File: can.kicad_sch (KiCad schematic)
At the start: 11 parts, among them U2 SN65HVD230

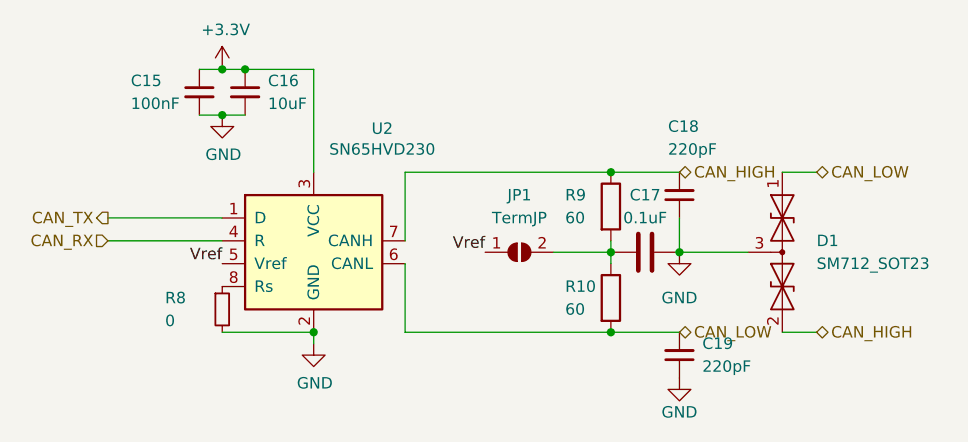
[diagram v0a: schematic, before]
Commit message: changed capacitor value and resistor footprints
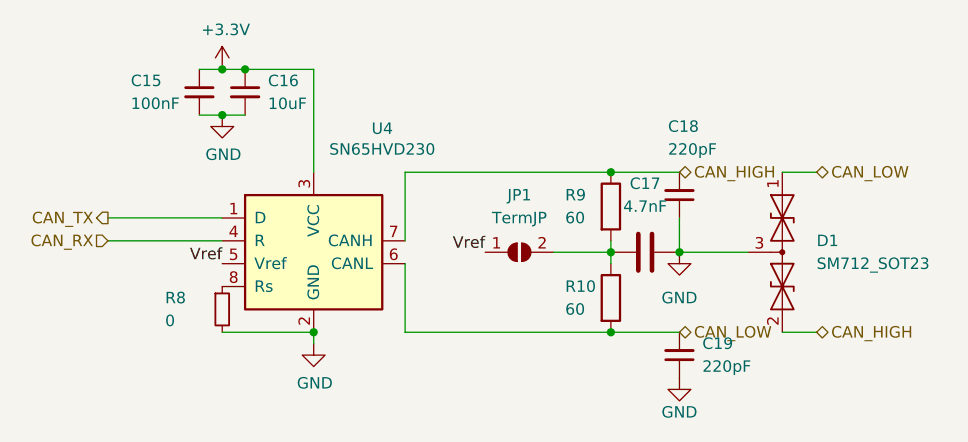
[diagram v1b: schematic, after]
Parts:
- C17: value 0.1uF -> 4.7nF
- JP1: footprint (none) -> Jumper:SolderJumper-2_P1.3mm_Open_RoundedPad1.0x1.5mm
- R10, R9: footprint Resistor_SMD:R_0402_1005Metric -> Resistor_SMD:R_0603_1608Metric
- renumbered U2 to U4
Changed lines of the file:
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@@
   (symbol (lib_id "power:GND") (at 134.62 99.06 0) (unit 1)
     (in_bom yes) (on_board yes) (fields_autoplaced)
-    (property "Reference" "#PWR026" (id 0) (at 134.62 105.41 0)
+    (property "Reference" "#PWR0130" (id 0) (at 134.62 105.41 0)
       (effects (font (size 1.27 1.27)) hide)
     )
@@
   (symbol (lib_id "power:+3.3V") (at 124.46 68.58 0) (unit 1)
     (in_bom yes) (on_board yes) (fields_autoplaced)
-    (property "Reference" "#PWR024" (id 0) (at 124.46 72.39 0)
+    (property "Reference" "#PWR0131" (id 0) (at 124.46 72.39 0)
       (effects (font (size 1.27 1.27)) hide)
     )
@@
   (symbol (lib_id "Interface_CAN_LIN:SN65HVD230") (at 134.62 87.63 0) (unit 1)
     (in_bom yes) (on_board yes) (fields_autoplaced)
-    (property "Reference" "U2" (id 0) (at 142.24 75.1586 0))
+    (property "Reference" "U4" (id 0) (at 142.24 75.1586 0))
     (property "Value" "SN65HVD230" (id 1) (at 142.24 77.47 0))
     (property "Footprint" "Package_SO:SOIC-8_3.9x4.9mm_P1.27mm" (id 2) (at 134.62 100.33 0)
@@
       (effects (font (size 1.27 1.27)) (justify left))
     )
-    (property "Footprint" "Resistor_SMD:R_0402_1005Metric" (id 2) (at 165.862 93.98 90)
+    (property "Footprint" "Resistor_SMD:R_0603_1608Metric" (id 2) (at 165.862 93.98 90)
       (effects (font (size 1.27 1.27)) hide)
     )
@@
       (effects (font (size 1.27 1.27)) (justify left))
     )
-    (property "Footprint" "Resistor_SMD:R_0402_1005Metric" (id 2) (at 165.862 83.82 90)
+    (property "Footprint" "Resistor_SMD:R_0603_1608Metric" (id 2) (at 165.862 83.82 90)
       (effects (font (size 1.27 1.27)) hide)
     )
@@
   (symbol (lib_id "Device:C") (at 171.45 88.9 90) (unit 1)
     (in_bom yes) (on_board yes) (fields_autoplaced)
-    (property "Reference" "C17" (id 0) (at 171.45 82.55 90))
-    (property "Value" "0.1uF" (id 1) (at 171.45 85.09 90))
+    (property "Reference" "C17" (id 0) (at 171.45 81.28 90))
+    (property "Value" "4.7nF" (id 1) (at 171.45 83.82 90))
     (property "Footprint" "Capacitor_SMD:C_0402_1005Metric" (id 2) (at 175.26 87.9348 0)
       (effects (font (size 1.27 1.27)) hide)
@@
     (property "Reference" "JP1" (id 0) (at 157.48 82.55 0))
     (property "Value" "TermJP" (id 1) (at 157.48 85.09 0))
-    (property "Footprint" "" (id 2) (at 157.48 88.9 0)
+    (property "Footprint" "Jumper:SolderJumper-2_P1.3mm_Open_RoundedPad1.0x1.5mm" (id 2) (at 157.48 88.9 0)
       (effects (font (size 1.27 1.27)) hide)
     )
@@
   )
   (symbol_instances
+    (path "/d85aebac-c325-42de-8c8e-5349542a2954"
+      (reference "#PWR025") (unit 1) (value "GND") (footprint "")
+    )
+    (path "/49208f5a-f73e-42f1-9d7d-382d975bd991"
+      (reference "#PWR027") (unit 1) (value "GND") (footprint "")
+    )
+    (path "/54c27e2d-52b9-4197-956b-7db5f761b4df"
+      (reference "#PWR028") (unit 1) (value "GND") (footprint "")
+    )
     (path "/00000000-0000-0000-0000-000061946eb3"
       (reference "#PWR0130") (unit 1) (value "GND") (footprint "")
@@
       (reference "#PWR0131") (unit 1) (value "+3.3V") (footprint "")
     )
+    (path "/759646bf-5c31-420e-aff7-2c1a28ce32e1"
+      (reference "C15") (unit 1) (value "100nF") (footprint "Capacitor_SMD:C_0402_1005Metric")
+    )
+    (path "/06b0d844-1c7a-43fd-b8a5-ad8e34e13aac"
+      (reference "C16") (unit 1) (value "10uF") (footprint "Capacitor_SMD:C_0402_1005Metric")
+    )
+    (path "/c905e3f6-13b1-4d5f-8bb5-930cfa107996"
+      (reference "C17") (unit 1) (value "4.7nF") (footprint "Capacitor_SMD:C_0402_1005Metric")
+    )
+    (path "/23622c20-4a70-4ee7-b39c-f5519633413f"
+      (reference "C18") (unit 1) (value "220pF") (footprint "Capacitor_SMD:C_0402_1005Metric")
+    )
+    (path "/f5a97da1-282d-43a4-ae5f-607cebde55a6"
+      (reference "C19") (unit 1) (value "220pF") (footprint "Capacitor_SMD:C_0402_1005Metric")
+    )
+    (path "/4717c16e-4caf-41db-976f-f247d2a86ecc"
+      (reference "D1") (unit 1) (value "SM712_SOT23") (footprint "Package_TO_SOT_SMD:SOT-23")
+    )
+    (path "/deb2b25e-9fb0-448e-88c5-95a67db1d371"
+      (reference "JP1") (unit 1) (value "TermJP") (footprint "Jumper:SolderJumper-2_P1.3mm_Open_RoundedPad1.0x1.5mm")
+    )
+    (path "/c0a35b75-0e83-4311-add3-5a3930110d30"
+      (reference "R8") (unit 1) (value "0") (footprint "Resistor_SMD:R_0603_1608Metric")
+    )
+    (path "/c4e42d16-8dbe-42af-a61a-faa72b95fe53"
+      (reference "R9") (unit 1) (value "60") (footprint "Resistor_SMD:R_0603_1608Metric")
+    )
+    (path "/c363df37-be76-44cd-846e-5e1010ee0d3e"
+      (reference "R10") (unit 1) (value "60") (footprint "Resistor_SMD:R_0603_1608Metric")
+    )
     (path "/00000000-0000-0000-0000-000061946ec3"

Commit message: changed usb port footprint to the combined SMD/THT one
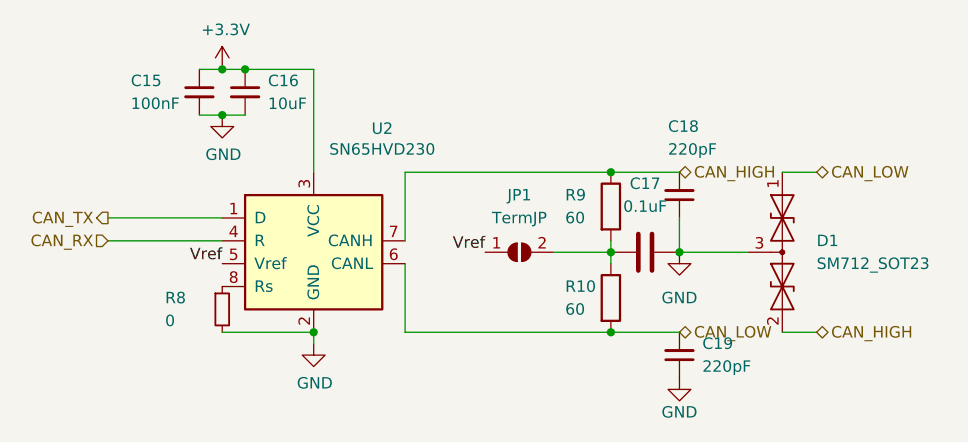
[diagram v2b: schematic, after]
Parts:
- C17: value 4.7nF -> 0.1uF
- R10, R9: footprint Resistor_SMD:R_0603_1608Metric -> Resistor_SMD:R_0402_1005Metric
- renumbered U4 to U2
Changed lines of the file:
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@@
   (symbol (lib_id "power:GND") (at 134.62 99.06 0) (unit 1)
     (in_bom yes) (on_board yes) (fields_autoplaced)
-    (property "Reference" "#PWR0130" (id 0) (at 134.62 105.41 0)
+    (property "Reference" "#PWR026" (id 0) (at 134.62 105.41 0)
       (effects (font (size 1.27 1.27)) hide)
     )
@@
   (symbol (lib_id "power:+3.3V") (at 124.46 68.58 0) (unit 1)
     (in_bom yes) (on_board yes) (fields_autoplaced)
-    (property "Reference" "#PWR0131" (id 0) (at 124.46 72.39 0)
+    (property "Reference" "#PWR024" (id 0) (at 124.46 72.39 0)
       (effects (font (size 1.27 1.27)) hide)
     )
@@
   (symbol (lib_id "Interface_CAN_LIN:SN65HVD230") (at 134.62 87.63 0) (unit 1)
     (in_bom yes) (on_board yes) (fields_autoplaced)
-    (property "Reference" "U4" (id 0) (at 142.24 75.1586 0))
+    (property "Reference" "U2" (id 0) (at 142.24 75.1586 0))
     (property "Value" "SN65HVD230" (id 1) (at 142.24 77.47 0))
     (property "Footprint" "Package_SO:SOIC-8_3.9x4.9mm_P1.27mm" (id 2) (at 134.62 100.33 0)
@@
       (effects (font (size 1.27 1.27)) (justify left))
     )
-    (property "Footprint" "Resistor_SMD:R_0603_1608Metric" (id 2) (at 165.862 93.98 90)
+    (property "Footprint" "Resistor_SMD:R_0402_1005Metric" (id 2) (at 165.862 93.98 90)
       (effects (font (size 1.27 1.27)) hide)
     )
@@
       (effects (font (size 1.27 1.27)) (justify left))
     )
-    (property "Footprint" "Resistor_SMD:R_0603_1608Metric" (id 2) (at 165.862 83.82 90)
+    (property "Footprint" "Resistor_SMD:R_0402_1005Metric" (id 2) (at 165.862 83.82 90)
       (effects (font (size 1.27 1.27)) hide)
     )
@@
     (in_bom yes) (on_board yes) (fields_autoplaced)
     (property "Reference" "C17" (id 0) (at 171.45 81.28 90))
-    (property "Value" "4.7nF" (id 1) (at 171.45 83.82 90))
+    (property "Value" "0.1uF" (id 1) (at 171.45 83.82 90))
     (property "Footprint" "Capacitor_SMD:C_0402_1005Metric" (id 2) (at 175.26 87.9348 0)
       (effects (font (size 1.27 1.27)) hide)

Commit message: updated some schematic values
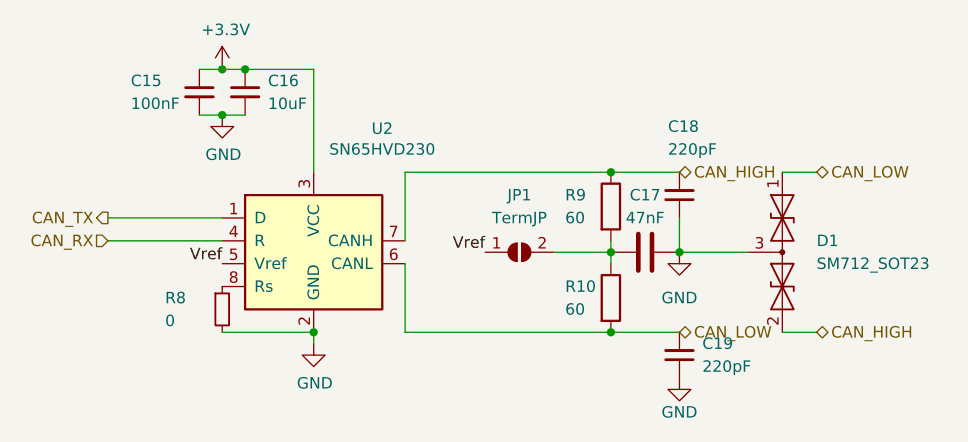
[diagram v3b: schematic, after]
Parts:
- C17: value 0.1uF -> 47nF
- R10, R9: footprint Resistor_SMD:R_0402_1005Metric -> Resistor_SMD:R_0603_1608Metric

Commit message: implemented fixes that were changed for ordering of nimbus flight electronics, tidied up layout and set up manufacturing constraints
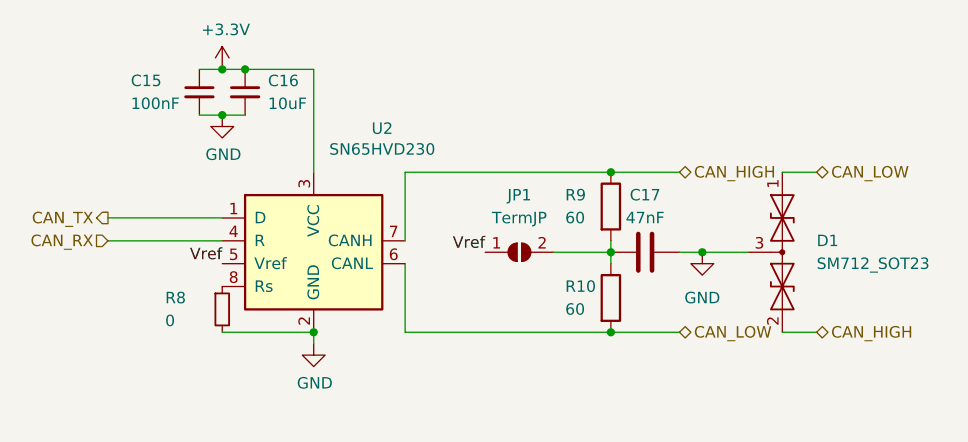
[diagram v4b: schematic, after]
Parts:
- removed C18, C19: 220pF, Capacitor_SMD:C_0402_1005Metric, symbol Device:C_Small
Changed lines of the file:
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@@
   (junction (at 167.64 80.01) (diameter 0) (color 0 0 0 0)
   )
-  (junction (at 175.26 88.9) (diameter 0) (color 0 0 0 0)
+  (junction (at 177.8 88.9) (diameter 0) (color 0 0 0 0)
   )
   (junction (at 167.64 97.79) (diameter 0) (color 0 0 0 0)
@@
     (stroke (width 0) (type default))
   )
+  (wire (pts (xy 177.8 88.9) (xy 182.88 88.9))
+    (stroke (width 0) (type default))
+  )
   (wire (pts (xy 121.92 73.66) (xy 124.46 73.66))
     (stroke (width 0) (type default))
@@
     (stroke (width 0) (type default))
   )
-  (wire (pts (xy 175.26 85.09) (xy 175.26 88.9))
-    (stroke (width 0) (type default))
-  )
   (wire (pts (xy 124.46 68.58) (xy 127 68.58))
     (stroke (width 0) (type default))
   )
-  (wire (pts (xy 175.26 88.9) (xy 182.88 88.9))
-    (stroke (width 0) (type default))
-  )
   (wire (pts (xy 111.76 87.63) (xy 124.46 87.63))
     (stroke (width 0) (type default))
@@
   )
   (wire (pts (xy 144.78 87.63) (xy 144.78 80.01))
+    (stroke (width 0) (type default))
+  )
+  (wire (pts (xy 177.8 88.9) (xy 175.26 88.9))
     (stroke (width 0) (type default))
   )
@@
     )
   )
-  (symbol (lib_id "Device:C_Small") (at 175.26 82.55 180) (unit 1)
-    (in_bom yes) (on_board yes) (dnp no)
-    (property "Reference" "C18" (at 173.99 74.93 0)
-      (effects (font (size 1.27 1.27)) (justify right))
-    )
-    (property "Value" "220pF" (at 173.99 77.47 0)
-      (effects (font (size 1.27 1.27)) (justify right))
-    )
-    (property "Footprint" "Capacitor_SMD:C_0402_1005Metric" (at 175.26 82.55 0)
-      (effects (font (size 1.27 1.27)) hide)
-    )
-    (property "Datasheet" "~" (at 175.26 82.55 0)
-      (effects (font (size 1.27 1.27)) hide)
-    )
-    (pin "1")
-    (pin "2")
-    (instances
-      (project "RicardoTemplate"
-        (path "/7db990e4-92e1-4f99-b4d2-435bbec1ba83/00000000-0000-0000-0000-000061942b9a"
-          (reference "C18") (unit 1)
-        )
-      )
-    )
-  )
   (symbol (lib_id "Diode:SM712_SOT23") (at 186.69 88.9 270) (unit 1)
     (in_bom yes) (on_board yes) (dnp no) (fields_autoplaced)
@@
     )
   )
-  (symbol (lib_id "power:GND") (at 175.26 88.9 0) (unit 1)
-    (in_bom yes) (on_board yes) (dnp no) (fields_autoplaced)
-    (property "Reference" "#PWR027" (at 175.26 95.25 0)
-      (effects (font (size 1.27 1.27)) hide)
-    )
-    (property "Value" "GND" (at 175.26 93.98 0)
-      (effects (font (size 1.27 1.27)))
-    )
-    (property "Footprint" "" (at 175.26 88.9 0)
-      (effects (font (size 1.27 1.27)) hide)
-    )
-    (property "Datasheet" "" (at 175.26 88.9 0)
+  (symbol (lib_id "power:GND") (at 177.8 88.9 0) (unit 1)
+    (in_bom yes) (on_board yes) (dnp no) (fields_autoplaced)
+    (property "Reference" "#PWR027" (at 177.8 95.25 0)
+      (effects (font (size 1.27 1.27)) hide)
+    )
+    (property "Value" "GND" (at 177.8 93.98 0)
+      (effects (font (size 1.27 1.27)))
+    )
+    (property "Footprint" "" (at 177.8 88.9 0)
+      (effects (font (size 1.27 1.27)) hide)
+    )
+    (property "Datasheet" "" (at 177.8 88.9 0)
       (effects (font (size 1.27 1.27)) hide)
     )
@@
         (path "/7db990e4-92e1-4f99-b4d2-435bbec1ba83/00000000-0000-0000-0000-000061942b9a"
           (reference "#PWR027") (unit 1)
-        )
-      )
-    )
-  )
-  (symbol (lib_id "power:GND") (at 175.26 102.87 0) (unit 1)
-    (in_bom yes) (on_board yes) (dnp no) (fields_autoplaced)
-    (property "Reference" "#PWR028" (at 175.26 109.22 0)
-      (effects (font (size 1.27 1.27)) hide)
-    )
-    (property "Value" "GND" (at 175.26 106.68 0)
-      (effects (font (size 1.27 1.27)))
-    )
-    (property "Footprint" "" (at 175.26 102.87 0)
-      (effects (font (size 1.27 1.27)) hide)
-    )
-    (property "Datasheet" "" (at 175.26 102.87 0)
-      (effects (font (size 1.27 1.27)) hide)
-    )
-    (pin "1")
-    (instances
-      (project "RicardoTemplate"
-        (path "/7db990e4-92e1-4f99-b4d2-435bbec1ba83/00000000-0000-0000-0000-000061942b9a"
-          (reference "#PWR028") (unit 1)
         )
       )
@@
         )
       )
-    )
-  )
-  (symbol (lib_id "Device:C_Small") (at 175.26 100.33 180) (unit 1)
-    (in_bom yes) (on_board yes) (dnp no) (fields_autoplaced)
-    (property "Reference" "C19" (at 177.8 99.0535 0)
-      (effects (font (size 1.27 1.27)) (justify right))
-    )
-    (property "Value" "220pF" (at 177.8 101.5935 0)
-      (effects (font (size 1.27 1.27)) (justify right))
-    )
-    (property "Footprint" "Capacitor_SMD:C_0402_1005Metric" (at 175.26 100.33 0)
-      (effects (font (size 1.27 1.27)) hide)
-    )
-    (property "Datasheet" "~" (at 175.26 100.33 0)
-      (effects (font (size 1.27 1.27)) hide)
-    )
-    (pin "1")
-    (pin "2")
-    (instances
-      (project "RicardoTemplate"
-        (path "/7db990e4-92e1-4f99-b4d2-435bbec1ba83/00000000-0000-0000-0000-000061942b9a"
-          (reference "C19") (unit 1)
-        )
-      )

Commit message: Added CAN LEDs and some general fixes noticed over the year
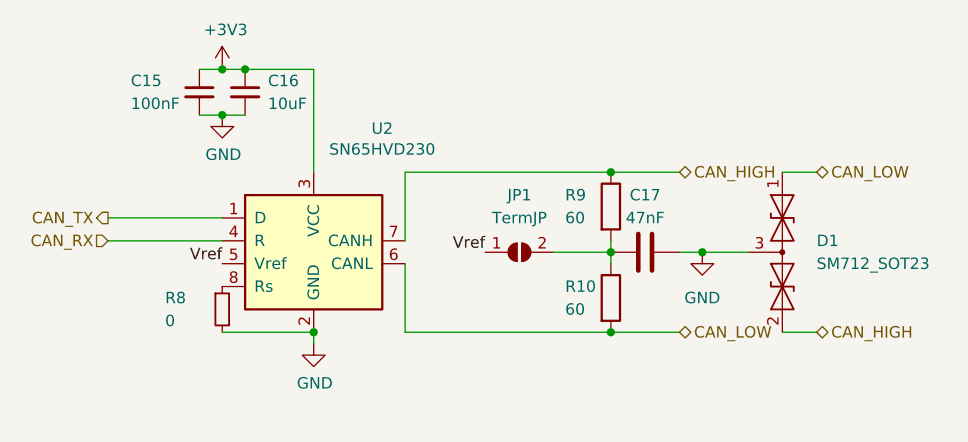
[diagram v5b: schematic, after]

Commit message: Fixed LED footprints assigned as resistors, added gitignore for locks and backups
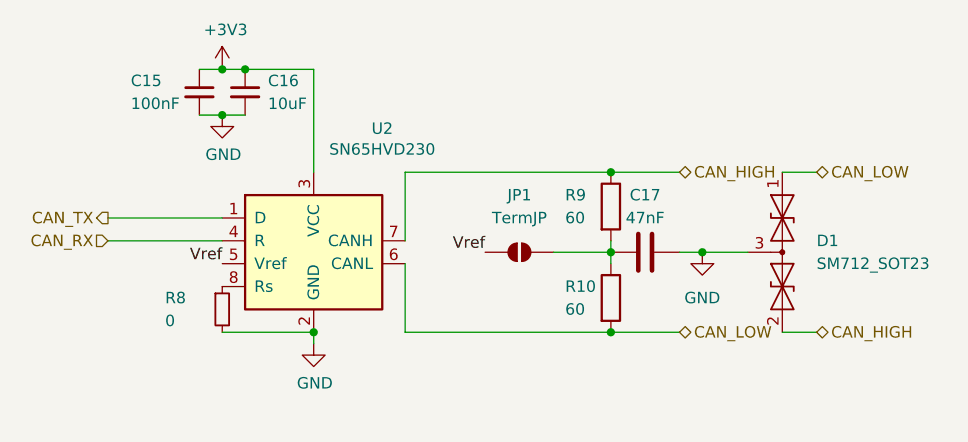
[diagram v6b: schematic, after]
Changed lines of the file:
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@@
 	(label "Vref"
 		(at 124.46 90.17 180)
-		(fields_autoplaced yes)
 		(effects
 			(font
@@
 	(label "Vref"
 		(at 153.67 88.9 180)
-		(fields_autoplaced yes)
 		(effects
 			(font
@@
 		(shape input)
 		(at 111.76 87.63 180)
-		(fields_autoplaced yes)
 		(effects
 			(font
@@
 		(shape bidirectional)
 		(at 175.26 80.01 0)
-		(fields_autoplaced yes)
 		(effects
 			(font
@@
 		(shape output)
 		(at 111.76 85.09 180)
-		(fields_autoplaced yes)
 		(effects
 			(font
@@
 		(shape bidirectional)
 		(at 190.5 97.79 0)
-		(fields_autoplaced yes)
 		(effects
 			(font
@@
 		(shape bidirectional)
 		(at 190.5 80.01 0)
-		(fields_autoplaced yes)
 		(effects
 			(font
@@
 		(shape bidirectional)
 		(at 175.26 97.79 0)
-		(fields_autoplaced yes)
 		(effects
 			(font
@@
 			)
 		)
-		(property "Description" ""
+		(property "Description" "Power symbol creates a global label with name \"GND\" , ground"
 			(at 134.62 99.06 0)
 			(effects
@@
 			)
 		)
-		(property "Description" ""
+		(property "Description" "Power symbol creates a global label with name \"+3.3V\""
 			(at 124.46 68.58 0)
 			(effects
@@
 			)
 		)
-		(property "Description" ""
+		(property "Description" "CAN Bus Transceivers, 3.3V, 1Mbps, Low-Power capabilities, SOIC-8"
 			(at 134.62 87.63 0)
 			(effects
@@
 			)
 		)
-		(property "Description" ""
+		(property "Description" "Unpolarized capacitor, small symbol"
 			(at 127 71.12 0)
 			(effects
@@
 			)
 		)
-		(property "Description" ""
+		(property "Description" "7V/12V, 600W Asymmetrical TVS Diode Array, SOT-23"
 			(at 186.69 88.9 0)
 			(effects
@@
 			)
 		)
-		(property "Description" ""
+		(property "Description" "Power symbol creates a global label with name \"GND\" , ground"
 			(at 177.8 88.9 0)
 			(effects
@@
 			)
 		)
-		(property "Description" ""
+		(property "Description" "Unpolarized capacitor, small symbol"
 			(at 121.92 71.12 0)
 			(effects
@@
 			)
 		)
-		(property "Description" ""
+		(property "Description" "Resistor, small symbol"
 			(at 124.46 95.25 0)
 			(effects
@@
 			)
 		)
-		(property "Description" ""
+		(property "Description" "Resistor"
 			(at 167.64 93.98 0)
 			(effects
@@
 			)
 		)
-		(property "Description" ""
+		(property "Description" "Resistor"
 			(at 167.64 83.82 0)
 			(effects
@@
 			)
 		)
-		(property "Description" ""
+		(property "Description" "Unpolarized capacitor"
 			(at 171.45 88.9 0)
 			(effects
@@
 			)
 		)
-		(property "Description" ""
+		(property "Description" "Power symbol creates a global label with name \"GND\" , ground"
 			(at 124.46 73.66 0)
 			(effects
@@
 			)
 		)
-		(property "Description" ""
+		(property "Description" "Solder Jumper, 2-pole, open"
 			(at 157.48 88.9 0)
 			(effects

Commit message: Fixed some footprint assignments, tidies up layout
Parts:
- JP1: footprint Jumper:SolderJumper-2_P1.3mm_Open_RoundedPad1.0x1.5mm -> iclr:SmallerSolderJP
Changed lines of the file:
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@@
 (kicad_sch
-	(version 20231120)
+	(version 20250114)
 	(generator "eeschema")
-	(generator_version "8.0")
+	(generator_version "9.0")
 	(paper "A4")
 	(junction
@@
 			)
 		)
-		(property "Footprint" "Jumper:SolderJumper-2_P1.3mm_Open_RoundedPad1.0x1.5mm"
+		(property "Footprint" "iclr:SmallerSolderJP"
 			(at 157.48 88.9 0)
 			(effects
